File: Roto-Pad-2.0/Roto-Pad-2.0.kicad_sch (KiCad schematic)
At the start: 11 parts, among them U1 Pico

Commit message: completed schematic, passes ERC
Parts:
- removed E2: ENCODER-RGB-SWITCH, Custom:Led Encoder, symbol SparkFun-Switches:ENCODER-RGB-SWITCH
- added S1: ENCODER-RGB-SWITCH, Custom:Led Encoder, symbol SparkFun-Switches:ENCODER-RGB-SWITCH
- R4, R5, R6, R7: footprint (none) -> PCM_Resistor_SMD_AKL:R_1206_3216Metric
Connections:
- net E1-A: now also S1.A
- net E1-B: now also S1.B
- net E1-sw: now also S1.3 (SW)
- net Neopixel/5v: now also S1.5 (+)
- net Neopixel/GND: now also U1.42 (GND), S1.C; no longer U1.38 (GND)
- net at R3.1: now also S1.4 (-B)
- net at R1.1: now also S1.1 (-R)
- net at R2.1: now also S1.2 (-G)
- removed net LED Display: U1.11 (GPIO8), U1.12 (GPIO9), U1.14 (GPIO10), U1.15 (GPIO11), U1.16 (GPIO12)
- no-connect marks 0 -> 17

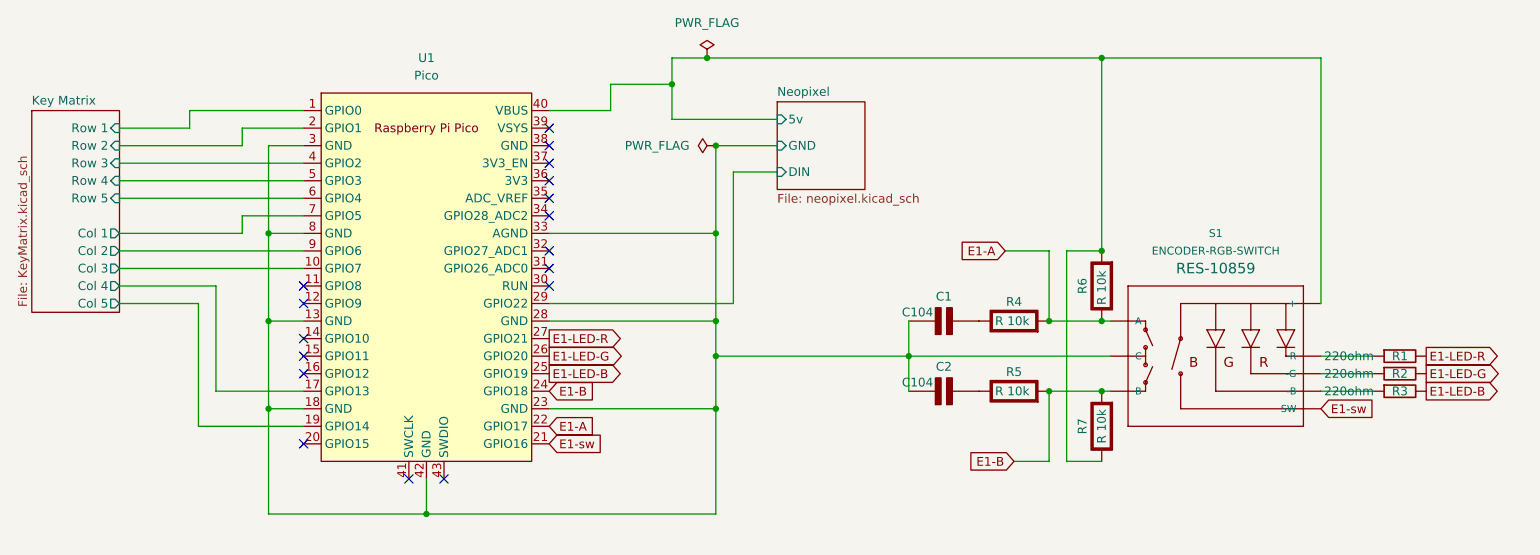
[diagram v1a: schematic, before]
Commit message: added more heirarchical sheets, debouncing
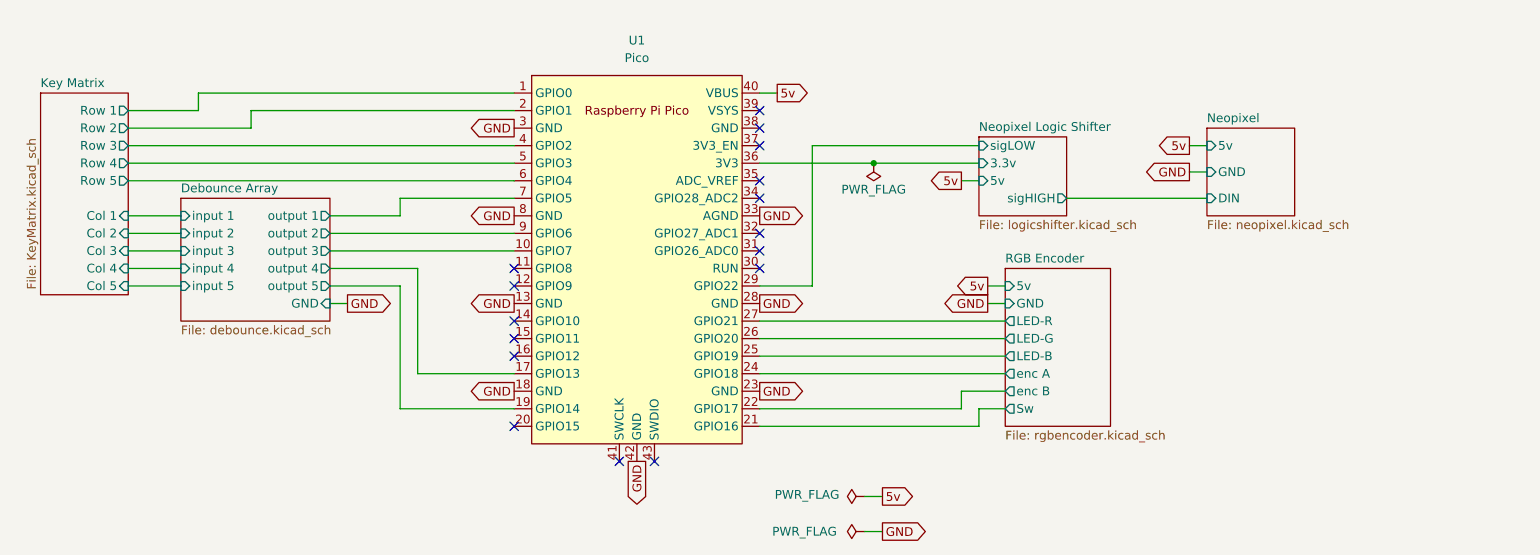
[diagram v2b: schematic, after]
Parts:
- removed C1, C2: C104, symbol PCM_Elektuur:C
- removed R1, R2, R3: 220ohm, PCM_Resistor_SMD_AKL:R_1206_3216Metric, symbol PCM_SL_Resistors:220ohm
- removed R4, R5, R6, R7: R 10k, PCM_Resistor_SMD_AKL:R_1206_3216Metric, symbol PCM_Elektuur:R
- removed S1: ENCODER-RGB-SWITCH, Custom:Led Encoder, symbol SparkFun-Switches:ENCODER-RGB-SWITCH
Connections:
- net Neopixel Logic Shifter/3.3v: now reaches U1.36 (3V3)
- net E1-A renamed RGB Encoder/enc B
- net E1-B renamed RGB Encoder/enc A
- net E1-LED-B renamed RGB Encoder/LED-B
- net E1-LED-G renamed RGB Encoder/LED-G
- net E1-LED-R renamed RGB Encoder/LED-R
- net E1-sw renamed RGB Encoder/Sw
- net Key Matrix/Col 1 renamed Debounce Array/output 1
- net Key Matrix/Col 2 renamed Debounce Array/output 2
- net Key Matrix/Col 3 renamed Debounce Array/output 3
- net Key Matrix/Col 4 renamed Debounce Array/output 4
- net Key Matrix/Col 5 renamed Debounce Array/output 5
- net Neopixel/5v renamed 5v
- net Neopixel/DIN renamed Neopixel Logic Shifter/sigLOW
- net Neopixel/GND renamed GND
- no-connect marks 17 -> 16
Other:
- added sheet Debounce Array (debounce.kicad_sch)
- added sheet Neopixel Logic Shifter (logicshifter.kicad_sch)
- added sheet RGB Encoder (rgbencoder.kicad_sch)
- moved on the sheet: U1
